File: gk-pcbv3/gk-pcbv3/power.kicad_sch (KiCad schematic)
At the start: 57 parts, among them J9 Conn_01x02, U18 LTC3112EDHD-PBF, U26 LT3380EUJM-PBF

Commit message: more v3 changes
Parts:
- added JP3: SolderJumper_3_Bridged12, Jumper:SolderJumper-3_P1.3mm_Open_Pad1.0x1.5mm_NumberLabels, symbol Jumper:SolderJumper_3_Bridged12
- added R74: 42.2k, Resistor_SMD:R_0603_1608Metric, symbol Device:R
- added R75, R76: 10k, Resistor_SMD:R_0603_1608Metric, symbol Device:R
- added TP16: TestPoint, TestPoint:TestPoint_Pad_D1.0mm, symbol Connector:TestPoint
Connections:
- net BOOST_VOUT: now also JP3.3 (B); no longer J9.2 (Pin_2), R79.2
- net GND: now also R74.2, R75.1, R76.2
- net VREGIN: now also JP3.1 (A)
- net at JP1.1 (A), U26.37 (EN_B4): now also R75.2
- net at JP1.3 (B), U26.9 (EN_L1): now also R76.1
- net at U18.7 (IOUT): now also R74.1, TP16.1
- new net: J9.2 (Pin_2), JP3.2 (C), R79.2
- no-connect marks 7 -> 6
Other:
- moved on the sheet: J9, R79

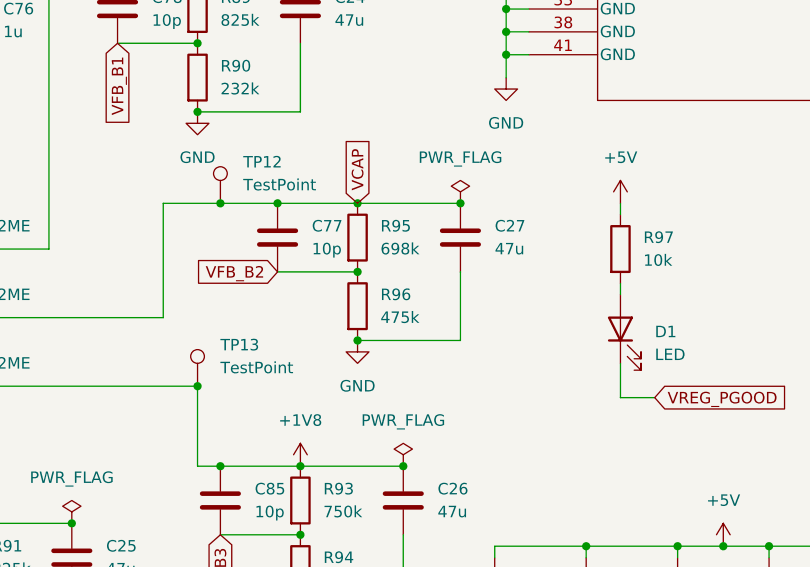
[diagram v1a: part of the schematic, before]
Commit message: fix vcap resistor divider
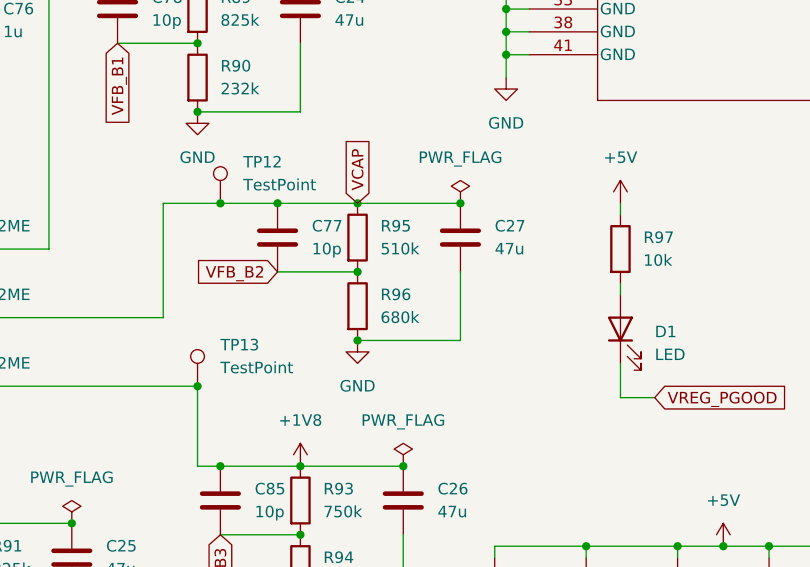
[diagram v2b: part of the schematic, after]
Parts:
- R95: value 698k -> 510k
- R96: value 475k -> 680k
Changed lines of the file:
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@@
 			)
 		)
-		(property "Value" "698k"
+		(property "Value" "510k"
 			(at 209.55 115.5699 0)
 			(effects
@@
 			)
 		)
-		(property "Value" "475k"
+		(property "Value" "680k"
 			(at 209.55 123.1899 0)
 			(effects

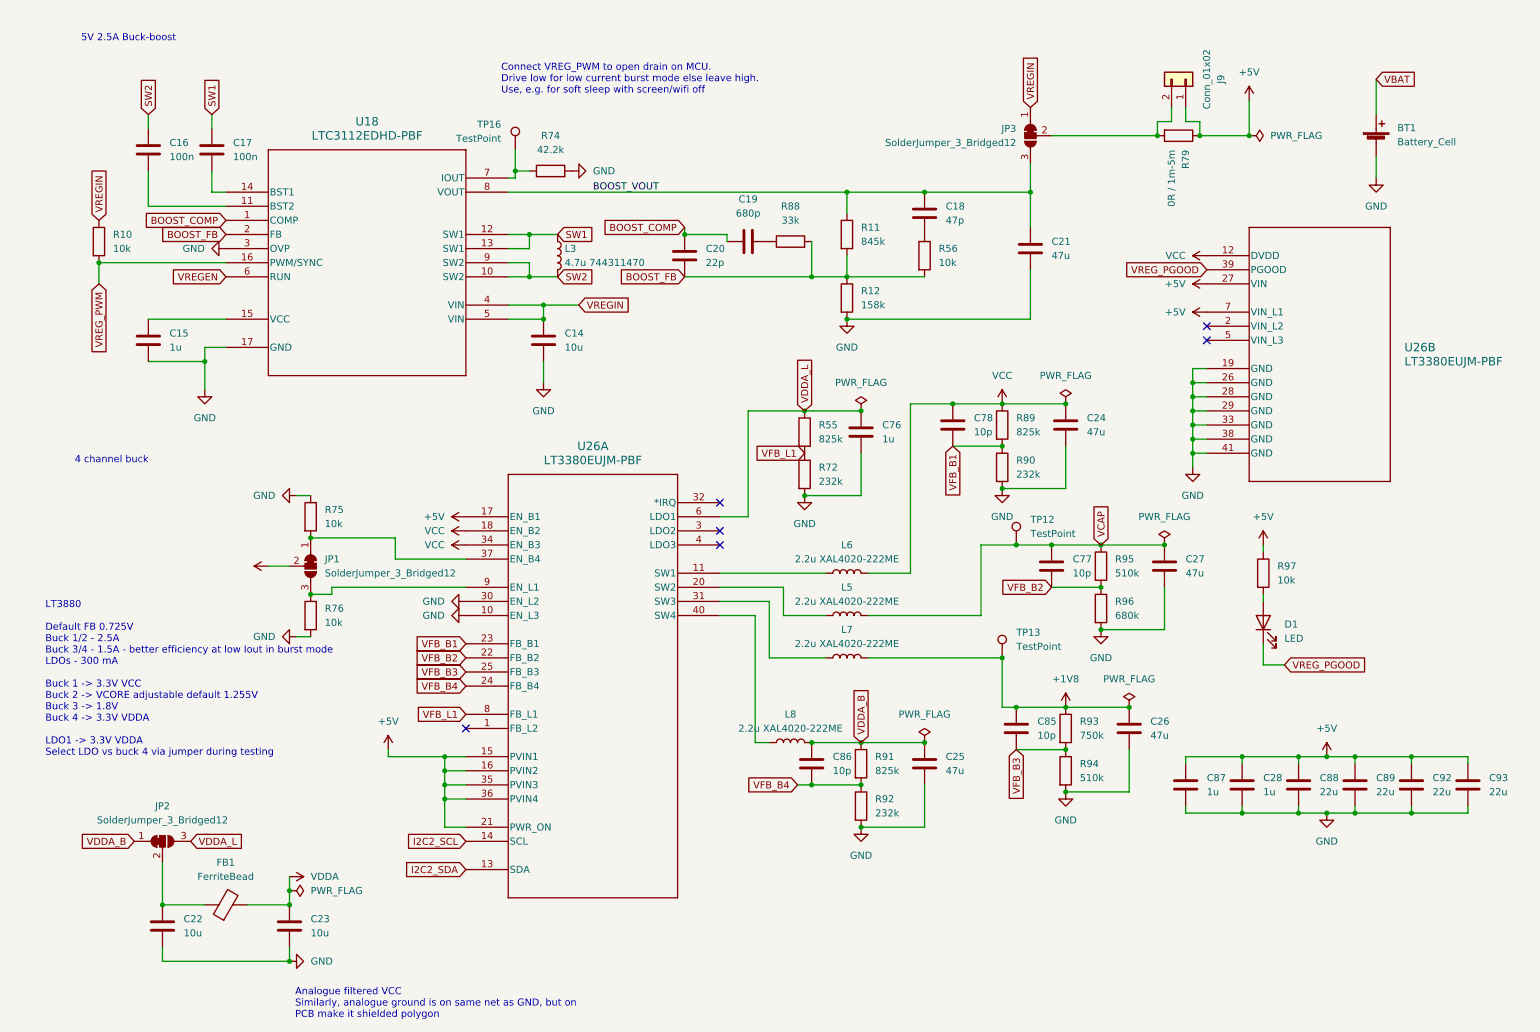
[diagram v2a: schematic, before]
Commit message: redesign for better signal integrity
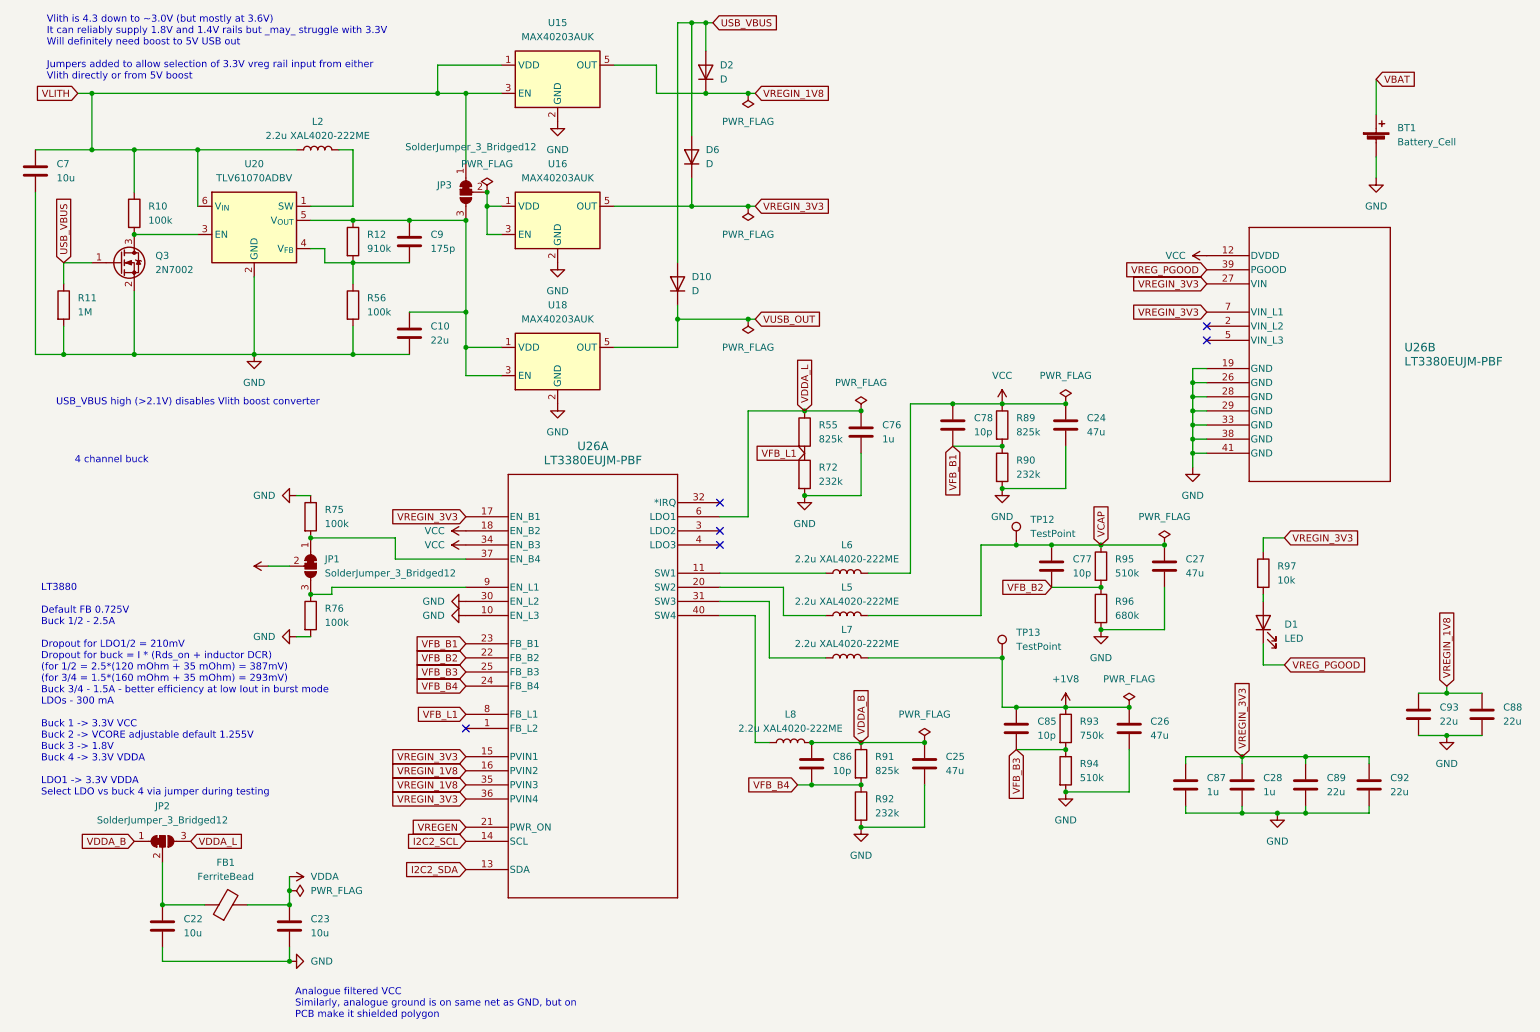
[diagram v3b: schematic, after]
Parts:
- removed C14: 10u, Capacitor_SMD:C_0805_2012Metric, symbol Device:C
- removed C15: 1u, Capacitor_SMD:C_0805_2012Metric, symbol Device:C
- removed C16, C17: 100n, Capacitor_SMD:C_0603_1608Metric, symbol Device:C
- removed C18: 47p, Capacitor_SMD:C_0603_1608Metric, symbol Device:C
- removed C19: 680p, Capacitor_SMD:C_0603_1608Metric, symbol Device:C
- removed C20: 22p, Capacitor_SMD:C_0603_1608Metric, symbol Device:C
- removed C21: 47u, Capacitor_SMD:C_1206_3216Metric, symbol Device:C
- removed J9: Conn_01x02, Connector_PinHeader_2.54mm:PinHeader_1x02_P2.54mm_Vertical, symbol Connector_Generic:Conn_01x02
- removed L3: 4.7u 744311470, Inductor_SMD:L_Wuerth_HCI-7030, symbol Device:L
- removed R74: 42.2k, Resistor_SMD:R_0603_1608Metric, symbol Device:R
- removed R79: 0R / 1m-5m, Resistor_SMD:R_2512_6332Metric, symbol Device:R
- removed R88: 33k, Resistor_SMD:R_0603_1608Metric, symbol Device:R
- removed TP16: TestPoint, TestPoint:TestPoint_Pad_D1.0mm, symbol Connector:TestPoint
- removed U18: LTC3112EDHD-PBF, STM32H7S7:LTC3112EDHD-PBF_ADI, symbol LTC3112:LTC3112EDHD-PBF
- added C10: 22u, Capacitor_SMD:C_0805_2012Metric, symbol Device:C
- added C7: 10u, Capacitor_SMD:C_0805_2012Metric, symbol Device:C
- added C9: 175p, Capacitor_SMD:C_0603_1608Metric, symbol Device:C
- added D10, D2, D6: D, Diode_SMD:D_SOD-128, symbol Device:D
- added L2: 2.2u XAL4020-222ME, Inductor_SMD:L_Coilcraft_XAL4020-XXX, symbol Device:L
- added Q3: 2N7002, Package_TO_SOT_SMD:SOT-23, symbol Transistor_FET:2N7002
- added U15, U16, U18: MAX40203AUK, Package_TO_SOT_SMD:SOT-23-5, symbol Analog_Switch:MAX40200AUK
- added U20: TLV61070ADBV, Package_TO_SOT_SMD:SOT-23-6, symbol Regulator_Switching:TLV61070ADBV
- R10, R56, R75, R76: value 10k -> 100k
- R11: value 845k -> 1M
- R12: value 158k -> 910k
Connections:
- net GND: now also R11.2, R56.2, C10.2, C7.2, Q3.2 (S), U15.2 (GND), U16.2 (GND), U18.2 (GND), U20.2 (GND); no longer R12.2
- net VREGEN: now also U26.21 (PWR_ON)
- net at JP3.2 (C): now also U16.1 (VDD), U16.3 (EN)
- net at R56.1: now also R12.2, C9.2, U20.4 (V_{FB})
- net +5V renamed VREGIN_3V3
- net VREGIN_3V3: now also D6.1 (K), U16.5 (OUT); no longer C88.1, C93.1, U26.16 (PVIN2), U26.21 (PWR_ON), U26.35 (PVIN3)
- removed net BOOST_FB: R11.2, R12.1, R56.2
- net BOOST_VOUT: no longer names the net of JP3.3 (B)
- net BOOST_VOUT: now also R12.1, C10.1, C9.1, U18.1 (VDD), U18.3 (EN), U20.5 (V_{OUT}); no longer R11.1
- net VREGIN renamed VLITH
- net VLITH: now also C7.1, L2.2, U15.1 (VDD), U15.3 (EN), U20.6 (V_{IN})
- net VREG_PWM: no longer names the net of R10.2
- net VREG_PWM: now also Q3.3 (D), U20.3 (EN)
- new net: L2.1, U20.1 (SW)
- new net USB_VBUS: D10.2 (A), D2.2 (A), D6.2 (A), Q3.1 (G), R11.1
- new net VREGIN_1V8: C88.1, C93.1, D2.1 (K), U15.5 (OUT), U26.16 (PVIN2), U26.35 (PVIN3)
- new net VUSB_OUT: D10.1 (K), U18.5 (OUT)
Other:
- note added: "LT3880 Default FB 0.725V Buck 1/2 - 2.5A Dropout for LDO1/2 = 210mV Dropout for buck = I * (Rds_on + inductor DCR) (for 1/2 = 2.5*(120 mOhm + 35 mOhm) = 387mV) (for 3/4 = 1.5*(160 mOhm + 35 mOhm) = 293mV) Buck 3/4 - 1.5A - better efficiency at low Iout in burst mode LDOs - 300 mA Buck 1 -> 3.3V VCC Buck 2 -> VCORE adjustable default 1.255V Buck 3 -> 1.8V Buck 4 -> 3.3V VDDA LDO1 -> 3.3V VDDA Sele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"
- note added: "USB_VBUS high (>2.1V) disables Vlith boost converter"
- note added: "Vlith is 4.3 down to ~3.0V (but mostly at 3.6V) It can reliably supply 1.8V and 1.4V rails but _may_ struggle with 3.3V Will definitely need boost to 5V USB out Jumpers added to allow selection of 3.3V vreg rail input from either Vlith directly or from 5V boost"
- note removed: "5V 2.5A Buck-boost"
- note removed: "Connect VREG_PWM to open drain on MCU. Drive low for low current burst mode else leave high. Use, e.g. for soft sleep with screen/wifi off"
- note removed: "LT3880 Default FB 0.725V Buck 1/2 - 2.5A Buck 3/4 - 1.5A - better efficiency at low Iout in burst mode LDOs - 300 mA Buck 1 -> 3.3V VCC Buck 2 -> VCORE adjustable default 1.255V Buck 3 -> 1.8V Buck 4 -> 3.3V VDDA LDO1 -> 3.3V VDDA Select LDO vs buck 4 via jumper during testing"
- moved on the sheet: C88, C89, C92, C93

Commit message: update schematics for new vreg design
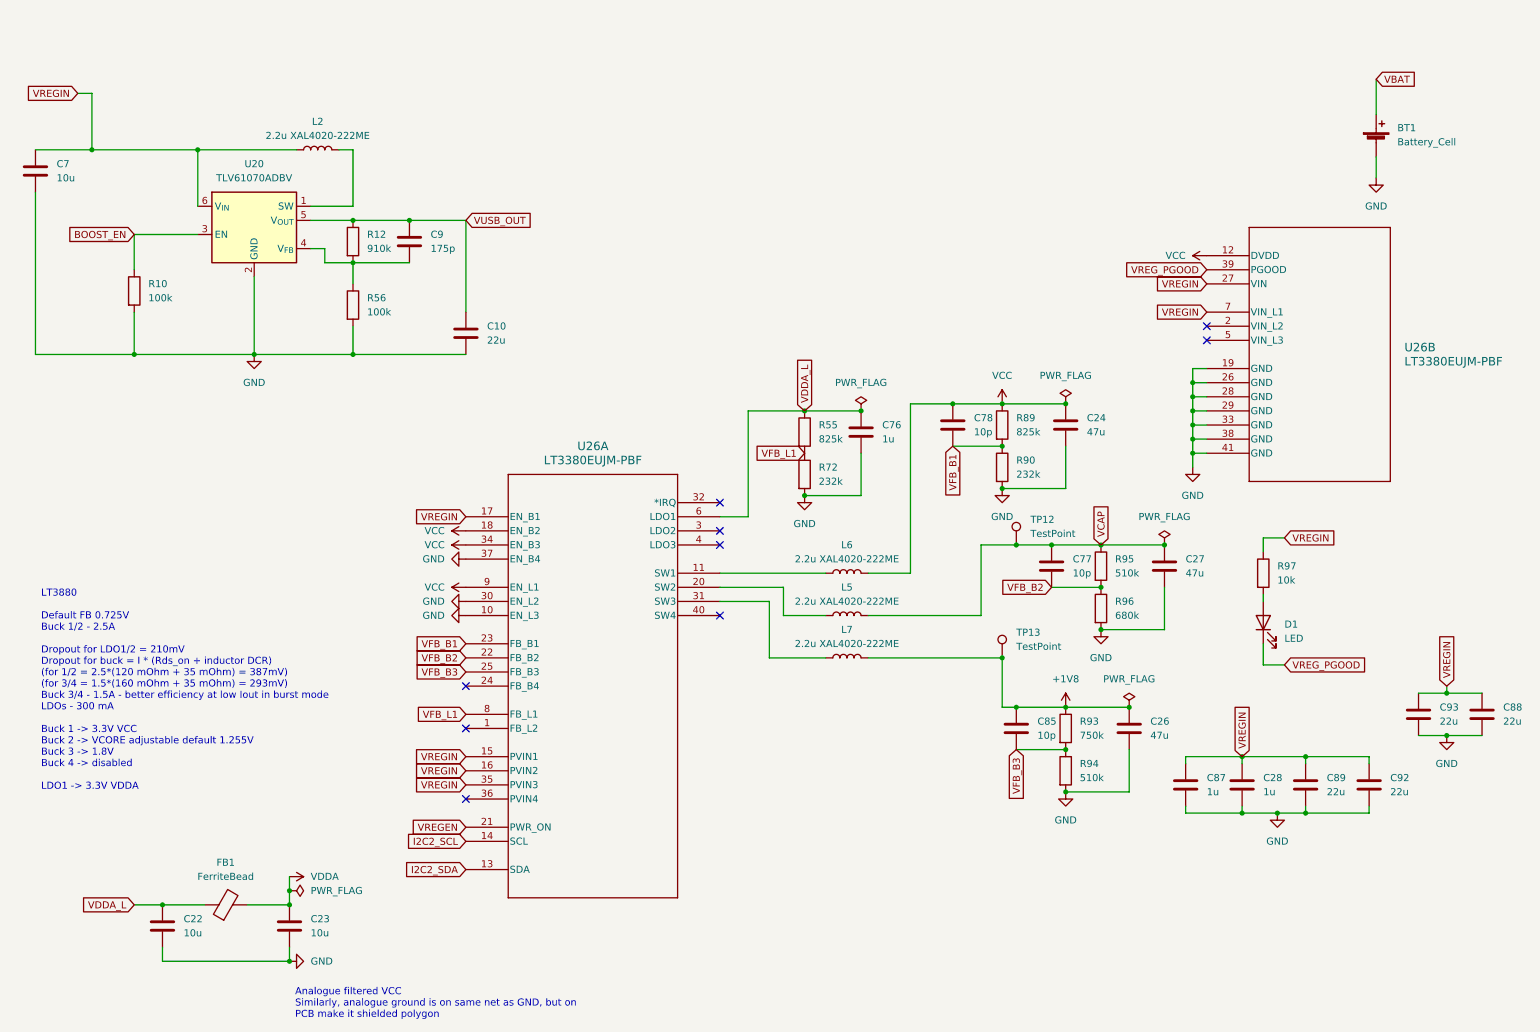
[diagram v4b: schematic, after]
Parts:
- removed C25: 47u, Capacitor_SMD:C_1206_3216Metric, symbol Device:C
- removed C86: 10p, Capacitor_SMD:C_0603_1608Metric, symbol Device:C
- removed D10, D2, D6: D, Diode_SMD:D_SOD-128, symbol Device:D
- removed JP1, JP2, JP3: SolderJumper_3_Bridged12, Jumper:SolderJumper-3_P1.3mm_Open_Pad1.0x1.5mm_NumberLabels, symbol Jumper:SolderJumper_3_Bridged12
- removed L8: 2.2u XAL4020-222ME, Inductor_SMD:L_Coilcraft_XAL4020-XXX, symbol Device:L
- removed Q3: 2N7002, Package_TO_SOT_SMD:SOT-23, symbol Transistor_FET:2N7002
- removed R11: 1M, Resistor_SMD:R_0603_1608Metric, symbol Device:R
- removed R75, R76: 100k, Resistor_SMD:R_0603_1608Metric, symbol Device:R
- removed R91: 825k, Resistor_SMD:R_0603_1608Metric, symbol Device:R
- removed R92: 232k, Resistor_SMD:R_0603_1608Metric, symbol Device:R
- removed U15, U16, U18: MAX40203AUK, Package_TO_SOT_SMD:SOT-23-5, symbol Analog_Switch:MAX40200AUK
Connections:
- net VREGIN_1V8 is gone; now on net VREGIN: C88.1, C93.1, U26.16 (PVIN2), U26.35 (PVIN3)
- net GND: now also R10.2, U26.37 (EN_B4)
- net VCC: now also U26.9 (EN_L1)
- net VDDA_L: now also C22.1, FB1.1
- net VUSB_OUT: now also C10.1, C9.1, R12.1, U20.5 (V_{OUT})
- net BOOST_EN: now reaches U20.3 (EN)
- net BOOST_EN: now also R10.1; no longer R10.2
- net VFB_B4: no longer names the net of U26.24 (FB_B4)
- net VLITH renamed VREGIN
- net VREGIN: now also C28.1, C87.1, C89.1, C92.1, R97.1, U26.15 (PVIN1), U26.17 (EN_B1), U26.27 (VIN), U26.7 (VIN_L1); no longer R10.1
- removed net VREGIN_3V3: C28.1, C87.1, C89.1, C92.1, R97.1, U26.15 (PVIN1), U26.17 (EN_B1), U26.27 (VIN), U26.36 (PVIN4), U26.7 (VIN_L1)
- no-connect marks 6 -> 9
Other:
- note added: "LT3880 Default FB 0.725V Buck 1/2 - 2.5A Dropout for LDO1/2 = 210mV Dropout for buck = I * (Rds_on + inductor DCR) (for 1/2 = 2.5*(120 mOhm + 35 mOhm) = 387mV) (for 3/4 = 1.5*(160 mOhm + 35 mOhm) = 293mV) Buck 3/4 - 1.5A - better efficiency at low Iout in burst mode LDOs - 300 mA Buck 1 -> 3.3V VCC Buck 2 -> VCORE adjustable default 1.255V Buck 3 -> 1.8V Buck 4 -> disabled LDO1 -> 3.3V VDDA"
- note removed: "4 channel buck"
- note removed: "LT3880 Default FB 0.725V Buck 1/2 - 2.5A Dropout for LDO1/2 = 210mV Dropout for buck = I * (Rds_on + inductor DCR) (for 1/2 = 2.5*(120 mOhm + 35 mOhm) = 387mV) (for 3/4 = 1.5*(160 mOhm + 35 mOhm) = 293mV) Buck 3/4 - 1.5A - better efficiency at low Iout in burst mode LDOs - 300 mA Buck 1 -> 3.3V VCC Buck 2 -> VCORE adjustable default 1.255V Buck 3 -> 1.8V Buck 4 -> 3.3V VDDA LDO1 -> 3.3V VDDA Sele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"
- note removed: "USB_VBUS high (>2.1V) disables Vlith boost converter"
- note removed: "Vlith is 4.3 down to ~3.0V (but mostly at 3.6V) It can reliably supply 1.8V and 1.4V rails but _may_ struggle with 3.3V Will definitely need boost to 5V USB out Jumpers added to allow selection of 3.3V vreg rail input from either Vlith directly or from 5V boost"
- moved on the sheet: C10

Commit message: new gerbers
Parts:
- removed C92: 22u, Capacitor_SMD:C_0805_2012Metric, symbol Device:C
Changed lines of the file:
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@@
 	)
 	(junction
-		(at 243.84 148.59)
-		(diameter 0)
-		(color 0 0 0 0)
-	)
-	(junction
 		(at 191.77 110.49)
 		(diameter 0)
@@
 	)
 	(junction
-		(at 243.84 158.75)
-		(diameter 0)
-		(color 0 0 0 0)
-	)
-	(junction
 		(at 198.12 110.49)
 		(diameter 0)
@@
 	(wire
 		(pts
-			(xy 255.27 148.59) (xy 255.27 149.86)
-		)
-		(stroke
-			(width 0)
-			(type default)
-		)
-	)
-	(wire
-		(pts
 			(xy 33.02 54.61) (xy 44.45 54.61)
 		)
@@
 	(wire
 		(pts
-			(xy 243.84 148.59) (xy 255.27 148.59)
-		)
-		(stroke
-			(width 0)
-			(type default)
-		)
-	)
-	(wire
-		(pts
 			(xy 38.1 185.42) (xy 60.96 185.42)
 		)
@@
 	(wire
 		(pts
-			(xy 243.84 158.75) (xy 255.27 158.75)
-		)
-		(stroke
-			(width 0)
-			(type default)
-		)
-	)
-	(wire
-		(pts
 			(xy 269.24 144.78) (xy 275.59 144.78)
 		)
@@
 	(wire
 		(pts
-			(xy 255.27 157.48) (xy 255.27 158.75)
-		)
-		(stroke
-			(width 0)
-			(type default)
-		)
-	)
-	(wire
-		(pts
 			(xy 25.4 39.37) (xy 44.45 39.37)
 		)
@@
 					(unit 1)
 				)
-			)
-		)
-	)
-	(symbol
-		(lib_id "Device:C")
-		(at 255.27 153.67 0)
-		(unit 1)
-		(exclude_from_sim no)
-		(in_bom yes)
-		(on_board yes)
-		(dnp no)
-		(fields_autoplaced yes)
-		(property "Reference" "C92"
-			(at 259.08 152.3999 0)
-			(effects
-				(font
-					(size 1.27 1.27)
-				)
-				(justify left)
-			)
-		)
-		(property "Value" "22u"
-			(at 259.08 154.9399 0)
-			(effects
-				(font
-					(size 1.27 1.27)
-				)
-				(justify left)
-			)
-		)
-		(property "Footprint" "Capacitor_SMD:C_0805_2012Metric"
-			(at 256.2352 157.48 0)
-			(effects
-				(font
-					(size 1.27 1.27)
-				)
-				(hide yes)
-			)
-		)
-		(property "Datasheet" "~"
-			(at 255.27 153.67 0)
-			(effects
-				(font
-					(size 1.27 1.27)
-				)
-				(hide yes)
-			)
-		)
-		(property "Description" "Unpolarized capacitor"
-			(at 255.27 153.67 0)
-			(effects
-				(font
-					(size 1.27 1.27)
-				)
-				(hide yes)
-			)
-		)
-		(pin "1"
-		)
-		(pin "2"
-		)
-		(instances
-			(project "gk-pcbv3"
-				(path "/08730ac6-6084-459f-bdf1-86b322355ede/3806a1c8-8d1e-497f-b14b-4fe834c820d3"
-					(reference "C92")
-					(unit 1)
-				)
